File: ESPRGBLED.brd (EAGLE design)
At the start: 22.5 x 25.7 mm, 25 parts

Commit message: minor layout stuff
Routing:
- net VCC: track 83.4 -> 80.4 mm
- net GND: track 11.8 -> 12.9 mm
- net N$6: track 18.7 -> 17.7 mm
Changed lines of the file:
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@@
 <setting verticaltext="up"/>
 </settings>
-<grid distance="12.5" unitdist="mil" unit="mm" style="lines" multiple="1" display="no" altdistance="6.25" altunitdist="mil" altunit="mil"/>
+<grid distance="0.1" unitdist="mm" unit="mm" style="dots" multiple="1" display="no" altdistance="0.05" altunitdist="mm" altunit="mm"/>
 <layers>
 <layer number="1" name="Top" color="4" fill="1" visible="yes" active="yes"/>
@@
 <layer number="46" name="Milling" color="3" fill="1" visible="no" active="yes"/>
 <layer number="47" name="Measures" color="7" fill="1" visible="no" active="yes"/>
-<layer number="48" name="Document" color="7" fill="1" visible="no" active="yes"/>
+<layer number="48" name="Document" color="7" fill="1" visible="yes" active="yes"/>
 <layer number="49" name="Reference" color="7" fill="1" visible="no" active="yes"/>
 <layer number="50" name="dxf" color="7" fill="1" visible="no" active="no"/>
@@
 </element>
 <element name="PWR1:T1" library="zetex" package="SOT223" value="" x="8.255" y="25.0825" smashed="yes" rot="R270">
-<attribute name="OC_FARNELL" value="1471058" x="8.255" y="25.0825" size="1.778" layer="27" rot="R270" display="off"/>
+<attribute name="OC_FARNELL" value="2069567" x="8.255" y="25.0825" size="1.778" layer="27" rot="R270" display="off"/>
 <attribute name="OC_NEWARK" value="unknown" x="8.255" y="25.0825" size="1.778" layer="27" rot="R270" display="off"/>
-<attribute name="MF" value="FAIRCHILD SEMICONDUCTOR" x="8.255" y="25.0825" size="1.778" layer="27" rot="R270" display="off"/>
-<attribute name="MPN" value="FDT439N" x="8.255" y="25.0825" size="1.778" layer="27" rot="R270" display="off"/>
+<attribute name="MF" value="NXP" x="8.255" y="25.0825" size="1.778" layer="27" rot="R270" display="off"/>
+<attribute name="MPN" value="PMT21EN" x="8.255" y="25.0825" size="1.778" layer="27" rot="R270" display="off"/>
 <attribute name="VALUE" x="6.9342" y="27.6225" size="1.27" layer="27" rot="R270"/>
 </element>
@@
 </element>
 <element name="PWR2:T1" library="zetex" package="SOT223" value="" x="8.255" y="18.0975" smashed="yes" rot="R270">
-<attribute name="OC_FARNELL" value="1471058" x="8.255" y="18.0975" size="1.778" layer="27" rot="R270" display="off"/>
+<attribute name="OC_FARNELL" value="2069567" x="8.255" y="18.0975" size="1.778" layer="27" rot="R270" display="off"/>
 <attribute name="OC_NEWARK" value="unknown" x="8.255" y="18.0975" size="1.778" layer="27" rot="R270" display="off"/>
-<attribute name="MF" value="FAIRCHILD SEMICONDUCTOR" x="8.255" y="18.0975" size="1.778" layer="27" rot="R270" display="off"/>
-<attribute name="MPN" value="FDT439N" x="8.255" y="18.0975" size="1.778" layer="27" rot="R270" display="off"/>
+<attribute name="MF" value="NXP" x="8.255" y="18.0975" size="1.778" layer="27" rot="R270" display="off"/>
+<attribute name="MPN" value="PMT21EN" x="8.255" y="18.0975" size="1.778" layer="27" rot="R270" display="off"/>
 <attribute name="VALUE" x="6.9342" y="20.6375" size="1.27" layer="27" rot="R270"/>
 </element>
@@
 </element>
 <element name="PWR3:T1" library="zetex" package="SOT223" value="" x="8.255" y="11.1125" smashed="yes" rot="R270">
-<attribute name="OC_FARNELL" value="1471058" x="8.255" y="11.1125" size="1.778" layer="27" rot="R270" display="off"/>
+<attribute name="OC_FARNELL" value="2069567" x="8.255" y="11.1125" size="1.778" layer="27" rot="R270" display="off"/>
 <attribute name="OC_NEWARK" value="unknown" x="8.255" y="11.1125" size="1.778" layer="27" rot="R270" display="off"/>
-<attribute name="MF" value="FAIRCHILD SEMICONDUCTOR" x="8.255" y="11.1125" size="1.778" layer="27" rot="R270" display="off"/>
-<attribute name="MPN" value="FDT439N" x="8.255" y="11.1125" size="1.778" layer="27" rot="R270" display="off"/>
+<attribute name="MF" value="NXP" x="8.255" y="11.1125" size="1.778" layer="27" rot="R270" display="off"/>
+<attribute name="MPN" value="PMT21EN" x="8.255" y="11.1125" size="1.778" layer="27" rot="R270" display="off"/>
 <attribute name="VALUE" x="6.9342" y="13.6525" size="1.27" layer="27" rot="R270"/>
 </element>
@@
 <via x="8.89" y="8.89" extent="1-16" drill="0.3302"/>
 <via x="8.89" y="12.7" extent="1-16" drill="0.3302"/>
-<via x="-0.3175" y="7.62" extent="1-16" drill="0.3302"/>
+<via x="-0.4175" y="7.62" extent="1-16" drill="0.3302"/>
 <via x="7.9375" y="22.86" extent="1-16" drill="0.3302"/>
 <via x="10.795" y="7.3025" extent="1-16" drill="0.3302"/>
+<wire x1="0.9525" y1="9.2075" x2="1.74625" y2="9.2075" width="0" layer="19" extent="1-16"/>
+<wire x1="1.74625" y1="9.2075" x2="1.74625" y2="9.31625" width="0" layer="19" extent="1-16"/>
+<wire x1="1.74625" y1="9.31625" x2="2.8575" y2="9.31625" width="0.48" layer="16"/>
 </signal>
 <signal name="VCC">
@@
 <wire x1="3.5052" y1="19.2786" x2="3.5052" y2="18.3642" width="0.1524" layer="16"/>
 <wire x1="6.1722" y1="21.9456" x2="3.5052" y2="19.2786" width="0.1524" layer="16"/>
-<wire x1="9.8298" y1="21.9456" x2="6.1722" y2="21.9456" width="0.1524" layer="16"/>
-<wire x1="10.0584" y1="22.1742" x2="9.8298" y2="21.9456" width="0.1524" layer="16"/>
-<wire x1="10.0584" y1="21.9456" x2="10.0584" y2="22.1742" width="0.1524" layer="1"/>
-<wire x1="11.1252" y1="20.8788" x2="10.0584" y2="21.9456" width="0.1524" layer="1"/>
+<wire x1="8.5598" y1="21.9456" x2="6.1722" y2="21.9456" width="0.1524" layer="16"/>
+<wire x1="8.7884" y1="22.1742" x2="8.5598" y2="21.9456" width="0.1524" layer="16"/>
+<wire x1="9.1059" y1="21.9456" x2="8.7884" y2="22.1742" width="0.1524" layer="1"/>
+<wire x1="9.5377" y1="21.5138" x2="9.1059" y2="21.9456" width="0.1524" layer="1"/>
 <wire x1="3.5052" y1="18.3642" x2="3.4925" y2="18.32" width="0.1524" layer="16"/>
 <wire x1="16.6878" y1="19.1262" x2="16.6878" y2="12.954" width="0.1524" layer="1"/>
 <wire x1="16.6878" y1="12.954" x2="16.66875" y2="12.93495" width="0.1524" layer="1"/>
 <wire x1="16.6878" y1="19.1262" x2="16.66875" y2="19.13275" width="0.1524" layer="1"/>
-<via x="10.0584" y="22.1742" extent="1-16" drill="0.3302"/>
+<via x="8.7884" y="22.1742" extent="1-16" drill="0.3302"/>
 <wire x1="10.795" y1="15.24" x2="10.16" y2="15.875" width="0.1524" layer="1"/>
 <wire x1="12.065" y1="15.24" x2="10.795" y2="15.24" width="0.1524" layer="1"/>
@@
 <wire x1="16.8275" y1="13.0175" x2="16.66875" y2="12.93495" width="0.1524" layer="1"/>
 <wire x1="9.525" y1="20.6375" x2="9.525" y2="16.51" width="0.1524" layer="1"/>
-<wire x1="11.1125" y1="20.6375" x2="9.525" y2="20.6375" width="0.1524" layer="1"/>
 <wire x1="9.8425" y1="15.875" x2="10.16" y2="15.875" width="0.1524" layer="1"/>
 <wire x1="9.525" y1="16.1925" x2="9.8425" y2="15.875" width="0.1524" layer="1"/>
@@
 <wire x1="0.25" y1="6.75" x2="0.3175" y2="6.653" width="0.1524" layer="1"/>
 <wire x1="16.75" y1="19.25" x2="16.66875" y2="19.13275" width="0.1524" layer="1"/>
-<wire x1="11.125" y1="20.625" x2="11.125" y2="20.875" width="0.1524" layer="1"/>
-<wire x1="11.125" y1="20.875" x2="11.1252" y2="20.8788" width="0.1524" layer="1"/>
-<wire x1="11.125" y1="20.625" x2="11.1125" y2="20.6375" width="0.1524" layer="1"/>
+<wire x1="9.5375" y1="20.9425" x2="9.5375" y2="21.1925" width="0.1524" layer="1"/>
+<wire x1="9.5375" y1="21.1925" x2="9.5377" y2="21.5138" width="0.1524" layer="1"/>
+<wire x1="9.5375" y1="20.9425" x2="9.525" y2="20.6375" width="0.1524" layer="1"/>
 </signal>
 <signal name="N$3">
@@
 <wire x1="9.6012" y1="19.431" x2="6.5532" y2="16.383" width="0.1524" layer="16"/>
 <wire x1="9.6012" y1="21.4122" x2="9.6012" y2="19.431" width="0.1524" layer="16"/>
-<wire x1="9.7536" y1="21.5646" x2="9.6012" y2="21.4122" width="0.1524" layer="16"/>
-<wire x1="10.287" y1="21.5646" x2="9.7536" y2="21.5646" width="0.1524" layer="16"/>
-<wire x1="10.668" y1="21.9456" x2="10.287" y2="21.5646" width="0.1524" layer="16"/>
-<wire x1="10.668" y1="22.4028" x2="10.668" y2="21.9456" width="0.1524" layer="16"/>
-<wire x1="6.7056" y1="26.3652" x2="10.668" y2="22.4028" width="0.1524" layer="16"/>
+<wire x1="9.7536" y1="22.8346" x2="9.6012" y2="21.4122" width="0.1524" layer="16"/>
+<wire x1="9.652" y1="22.8346" x2="9.7536" y2="22.8346" width="0.1524" layer="16"/>
+<wire x1="9.7155" y1="22.8981" x2="9.652" y2="22.8346" width="0.1524" layer="16"/>
+<wire x1="9.7155" y1="23.3553" x2="9.7155" y2="22.8981" width="0.1524" layer="16"/>
+<wire x1="6.7056" y1="26.3652" x2="9.7155" y2="23.3553" width="0.1524" layer="16"/>
 <wire x1="6.1722" y1="26.3652" x2="6.7056" y2="26.3652" width="0.1524" layer="1"/>
 <wire x1="5.1816" y1="27.3558" x2="6.1722" y2="26.3652" width="0.1524" layer="1"/>
@@
 <contactref element="JMP1" pad="2"/>
 <contactref element="MDL1" pad="3"/>
-<wire x1="0.125" y1="5.625" x2="0.25" y2="5.625" width="0.1524" layer="1"/>
-<wire x1="-0.5" y1="5" x2="0.125" y2="5.625" width="0.1524" layer="1"/>
-<wire x1="-0.5" y1="4.25" x2="-0.5" y2="5" width="0.1524" layer="1"/>
-<wire x1="1.25" y1="4.25" x2="-0.5" y2="4.25" width="0.1524" layer="16"/>
+<wire x1="0.025" y1="5.625" x2="0.15" y2="5.625" width="0.1524" layer="1"/>
+<wire x1="-0.5" y1="5.1" x2="0.025" y2="5.625" width="0.1524" layer="1"/>
+<wire x1="-0.5" y1="4.15" x2="-0.5" y2="5.1" width="0.1524" layer="1"/>
+<wire x1="1.25" y1="4.25" x2="-0.5" y2="4.15" width="0.1524" layer="16"/>
 <wire x1="2.375" y1="5.375" x2="1.25" y2="4.25" width="0.1524" layer="16"/>
 <wire x1="4.5" y1="5.375" x2="2.375" y2="5.375" width="0.1524" layer="16"/>
@@
 <wire x1="5" y1="8.25" x2="5.75" y2="7.5" width="0.1524" layer="16"/>
 <wire x1="3.5" y1="8.25" x2="5" y2="8.25" width="0.1524" layer="16"/>
-<wire x1="0.25" y1="5.625" x2="0.3175" y2="5.715" width="0.1524" layer="1"/>
+<wire x1="0.15" y1="5.625" x2="0.3175" y2="5.715" width="0.1524" layer="1"/>
 <wire x1="3.5" y1="8.25" x2="3.4925" y2="8.32" width="0.1524" layer="16"/>
-<via x="-0.5" y="4.25" extent="1-16" drill="0.3302"/>
+<via x="-0.5" y="4.15" extent="1-16" drill="0.3302"/>
 </signal>
 <signal name="N$11">

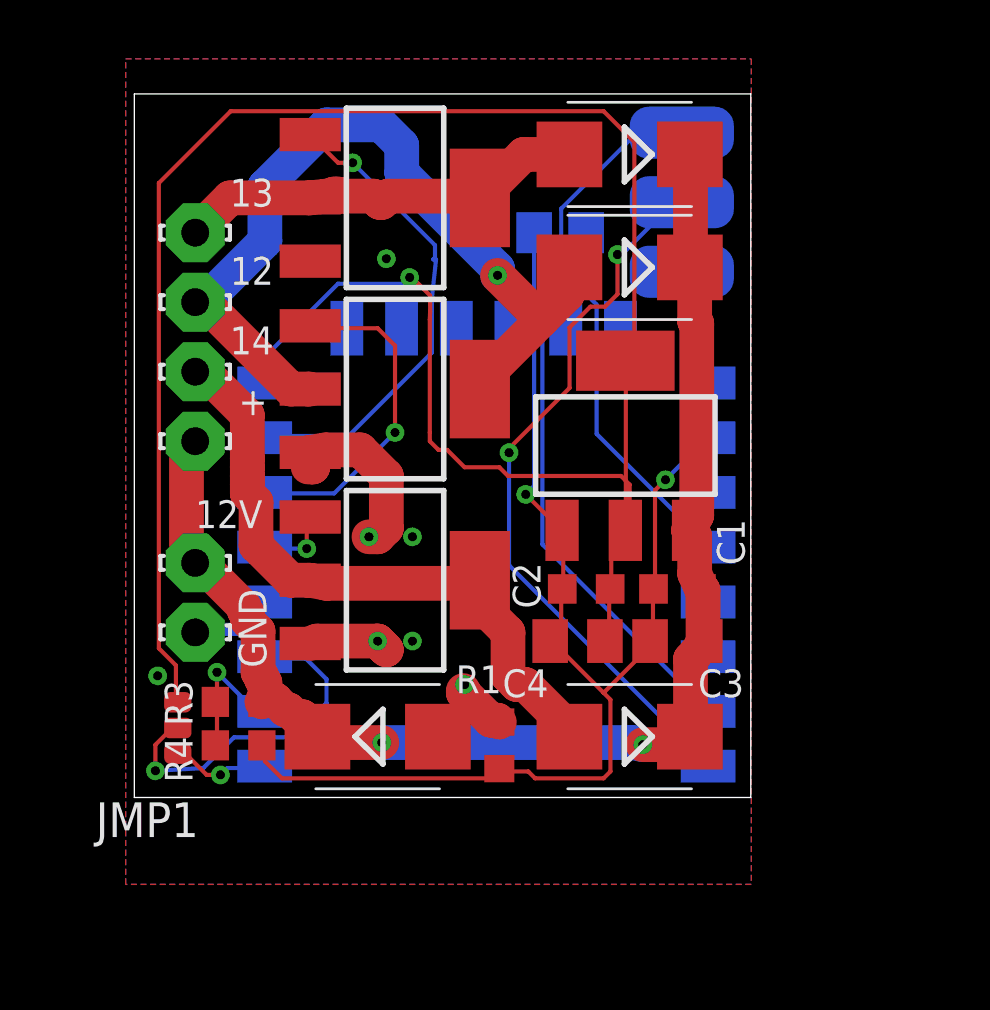
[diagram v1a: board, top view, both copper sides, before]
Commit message: first working over http
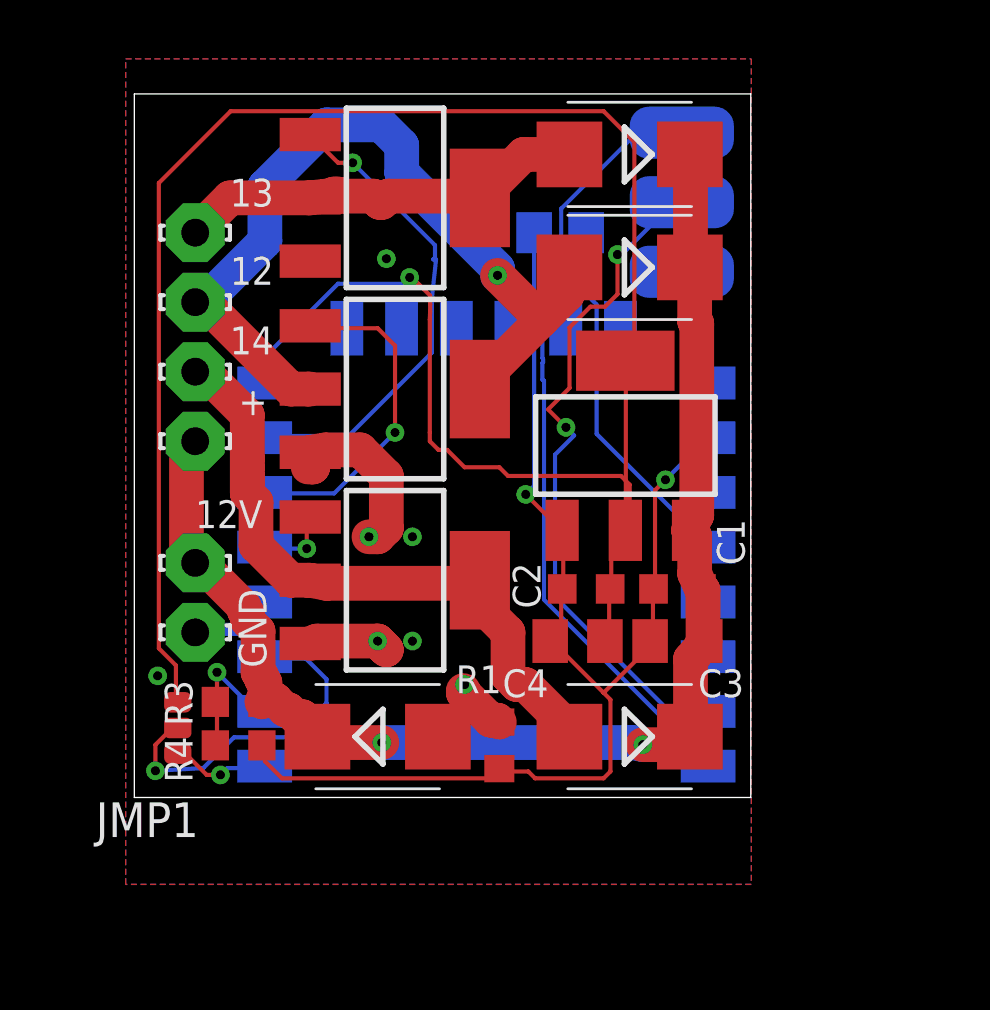
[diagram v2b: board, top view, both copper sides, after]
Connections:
- net N$7: now also MDL1.16; no longer MDL1.15
- net N$8: now also MDL1.15; no longer MDL1.16
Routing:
- net N$7: track 26.7 -> 29.3 mm
- net N$8: track 27.6 -> 25.8 mm
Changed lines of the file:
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@@
 <setting verticaltext="up"/>
 </settings>
-<grid distance="0.1" unitdist="mm" unit="mm" style="dots" multiple="1" display="no" altdistance="0.05" altunitdist="mm" altunit="mm"/>
+<grid distance="1" unitdist="mil" unit="mil" style="dots" multiple="1" display="no" altdistance="0.05" altunitdist="mm" altunit="mm"/>
 <layers>
 <layer number="1" name="Top" color="4" fill="1" visible="yes" active="yes"/>
@@
 <layer number="19" name="Unrouted" color="6" fill="1" visible="yes" active="yes"/>
 <layer number="20" name="Dimension" color="15" fill="1" visible="yes" active="yes"/>
-<layer number="21" name="tPlace" color="7" fill="1" visible="yes" active="yes"/>
+<layer number="21" name="tPlace" color="7" fill="1" visible="no" active="yes"/>
 <layer number="22" name="bPlace" color="7" fill="1" visible="yes" active="yes"/>
-<layer number="23" name="tOrigins" color="15" fill="1" visible="yes" active="yes"/>
-<layer number="24" name="bOrigins" color="15" fill="1" visible="yes" active="yes"/>
+<layer number="23" name="tOrigins" color="15" fill="1" visible="no" active="yes"/>
+<layer number="24" name="bOrigins" color="15" fill="1" visible="no" active="yes"/>
 <layer number="25" name="tNames" color="7" fill="1" visible="no" active="yes"/>
 <layer number="26" name="bNames" color="7" fill="1" visible="no" active="yes"/>
@@
 <layer number="46" name="Milling" color="3" fill="1" visible="no" active="yes"/>
 <layer number="47" name="Measures" color="7" fill="1" visible="no" active="yes"/>
-<layer number="48" name="Document" color="7" fill="1" visible="yes" active="yes"/>
+<layer number="48" name="Document" color="7" fill="1" visible="no" active="yes"/>
 <layer number="49" name="Reference" color="7" fill="1" visible="no" active="yes"/>
 <layer number="50" name="dxf" color="7" fill="1" visible="no" active="no"/>
-<layer number="51" name="tDocu" color="7" fill="1" visible="yes" active="yes"/>
+<layer number="51" name="tDocu" color="7" fill="1" visible="no" active="yes"/>
 <layer number="52" name="bDocu" color="7" fill="1" visible="yes" active="yes"/>
 <layer number="53" name="tGND_GNDA" color="7" fill="1" visible="no" active="no"/>
@@
 <via x="7.9375" y="22.86" extent="1-16" drill="0.3302"/>
 <via x="10.795" y="7.3025" extent="1-16" drill="0.3302"/>
-<wire x1="0.9525" y1="9.2075" x2="1.74625" y2="9.2075" width="0" layer="19" extent="1-16"/>
-<wire x1="1.74625" y1="9.2075" x2="1.74625" y2="9.31625" width="0" layer="19" extent="1-16"/>
 <wire x1="1.74625" y1="9.31625" x2="2.8575" y2="9.31625" width="0.48" layer="16"/>
 </signal>
@@
 <signal name="N$7">
 <contactref element="U$3" pad="SIG"/>
-<contactref element="MDL1" pad="15"/>
-<wire x1="19.6596" y1="6.3246" x2="19.6925" y2="6.32" width="0.1524" layer="16"/>
-<wire x1="13.6398" y1="12.4206" x2="19.6596" y2="6.4008" width="0.1524" layer="16"/>
-<wire x1="13.6398" y1="22.3266" x2="13.6398" y2="12.4206" width="0.1524" layer="16"/>
-<wire x1="14.3256" y1="23.0124" x2="13.6398" y2="22.3266" width="0.1524" layer="16"/>
 <wire x1="14.3256" y1="24.6888" x2="14.3256" y2="23.0124" width="0.1524" layer="16"/>
 <wire x1="17.0688" y1="27.432" x2="14.3256" y2="24.6888" width="0.1524" layer="16"/>
 <wire x1="18.669" y1="27.432" x2="17.0688" y2="27.432" width="0.1524" layer="16"/>
-<wire x1="19.6596" y1="6.4008" x2="19.6925" y2="6.32" width="0.1524" layer="16"/>
 <wire x1="18.669" y1="27.432" x2="18.7325" y2="27.46375" width="0.1524" layer="16"/>
+<contactref element="MDL1" pad="16"/>
+<wire x1="13.7" y1="10.4" x2="13.7" y2="18.4" width="0.15" layer="16"/>
+<wire x1="18.4" y1="5.7" x2="13.7" y2="10.4" width="0.15" layer="16"/>
+<wire x1="18.4" y1="5.6" x2="18.4" y2="5.7" width="0.15" layer="16"/>
+<wire x1="18.6" y1="5.4" x2="18.4" y2="5.6" width="0.15" layer="16"/>
+<wire x1="18.7" y1="5.4" x2="18.6" y2="5.4" width="0.15" layer="16"/>
+<wire x1="18.8" y1="5.3" x2="18.7" y2="5.4" width="0.15" layer="16"/>
+<wire x1="18.8" y1="4.4" x2="18.8" y2="5.3" width="0.15" layer="16"/>
+<wire x1="18.9" y1="4.3" x2="18.8" y2="4.4" width="0.15" layer="16"/>
+<wire x1="19.6" y1="4.3" x2="18.9" y2="4.3" width="0.15" layer="16"/>
+<wire x1="19.6" y1="4.3" x2="19.6925" y2="4.32" width="0.15" layer="16"/>
+<wire x1="13.7668" y1="22.3012" x2="13.7668" y2="21.8694" width="0.15" layer="16"/>
+<wire x1="14.2748" y1="22.8092" x2="13.7668" y2="22.3012" width="0.15" layer="16"/>
+<wire x1="14.2748" y1="22.9616" x2="14.2748" y2="22.8092" width="0.15" layer="16"/>
+<wire x1="14.2748" y1="22.9616" x2="14.3256" y2="23.0124" width="0.15" layer="16"/>
+<wire x1="13.6398" y1="21.7424" x2="13.7668" y2="21.8694" width="0.15" layer="16"/>
+<wire x1="13.6398" y1="21.5646" x2="13.6398" y2="21.7424" width="0.15" layer="16"/>
+<wire x1="13.6652" y1="21.5392" x2="13.6398" y2="21.5646" width="0.15" layer="16"/>
+<wire x1="13.6652" y1="21.4376" x2="13.6652" y2="21.5392" width="0.15" layer="16"/>
+<wire x1="13.6398" y1="21.4122" x2="13.6652" y2="21.4376" width="0.15" layer="16"/>
+<wire x1="13.6398" y1="19.2278" x2="13.6398" y2="21.4122" width="0.15" layer="16"/>
+<wire x1="13.6652" y1="19.2024" x2="13.6398" y2="19.2278" width="0.15" layer="16"/>
+<wire x1="13.6652" y1="19.0754" x2="13.6652" y2="19.2024" width="0.15" layer="16"/>
+<wire x1="13.6398" y1="19.05" x2="13.6652" y2="19.0754" width="0.15" layer="16"/>
+<wire x1="13.6398" y1="18.4404" x2="13.6398" y2="19.05" width="0.15" layer="16"/>
+<wire x1="13.6398" y1="18.4404" x2="13.7" y2="18.4" width="0.15" layer="16"/>
 </signal>
 <signal name="N$8">
 <contactref element="U$3" pad="5V"/>
-<contactref element="MDL1" pad="16"/>
-<wire x1="19.6596" y1="4.3434" x2="19.6925" y2="4.32" width="0.1524" layer="16"/>
 <wire x1="18.669" y1="25.6794" x2="18.7325" y2="24.92375" width="0.1524" layer="16"/>
-<wire x1="12.4206" y1="11.6586" x2="19.6596" y2="4.4196" width="0.1524" layer="16"/>
-<wire x1="12.4206" y1="15.7734" x2="12.4206" y2="11.6586" width="0.1524" layer="16"/>
-<wire x1="12.4206" y1="15.9258" x2="12.4206" y2="15.7734" width="0.1524" layer="1"/>
-<wire x1="14.6304" y1="18.1356" x2="12.4206" y2="15.9258" width="0.1524" layer="1"/>
+<wire x1="14.6304" y1="18.1356" x2="13.8474" y2="17.3526" width="0.1524" layer="1"/>
 <wire x1="14.6304" y1="20.3454" x2="14.6304" y2="18.1356" width="0.1524" layer="1"/>
 <wire x1="15.3924" y1="21.1074" x2="14.6304" y2="20.3454" width="0.1524" layer="1"/>
@@
 <wire x1="18.4404" y1="24.9174" x2="16.5354" y2="23.0124" width="0.1524" layer="16"/>
 <wire x1="18.669" y1="24.9174" x2="18.4404" y2="24.9174" width="0.1524" layer="16"/>
-<wire x1="19.6596" y1="4.4196" x2="19.6925" y2="4.32" width="0.1524" layer="16"/>
 <wire x1="18.669" y1="24.9174" x2="18.7325" y2="24.92375" width="0.1524" layer="16"/>
-<via x="12.4206" y="15.7734" extent="1-16" drill="0.3302"/>
 <via x="16.383" y="23.0124" extent="1-16" drill="0.3302"/>
+<contactref element="MDL1" pad="15"/>
+<wire x1="14.5" y1="16.7" x2="14.8" y2="16.4" width="0.15" layer="16"/>
+<wire x1="13.8474" y1="17.3526" x2="14.5" y2="16.7" width="0.15" layer="1"/>
+<wire x1="14.1" y1="15.7" x2="14.8" y2="16.4" width="0.15" layer="16"/>
+<wire x1="14.1" y1="10.5" x2="14.1" y2="15.7" width="0.15" layer="16"/>
+<wire x1="18.3" y1="6.3" x2="14.1" y2="10.5" width="0.15" layer="16"/>
+<wire x1="19.6" y1="6.3" x2="18.3" y2="6.3" width="0.15" layer="16"/>
+<wire x1="19.6" y1="6.3" x2="19.6925" y2="6.32" width="0.15" layer="16"/>
+<via x="14.5" y="16.7" extent="1-16" drill="0.3302"/>
 </signal>
 <signal name="N$2">
